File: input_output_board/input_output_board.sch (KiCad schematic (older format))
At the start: 18 parts, among them J1 Neutrik_NCJ6FA-H, J2 Neutrik_NCJ6FA-H, J3 Neutrik_NCJ6FA-H, J4 Neutrik_NCJ6FA-H, J5 Molex_SL_01x04_Male, J6 Conn_02x08_Odd_Even, J7 Molex_SL_01x04_Male, J8 AudioJack3, K1 G6S-2, K2 G6S-2, K3 G6S-2, K4 G6S-2, K5 G6S-2

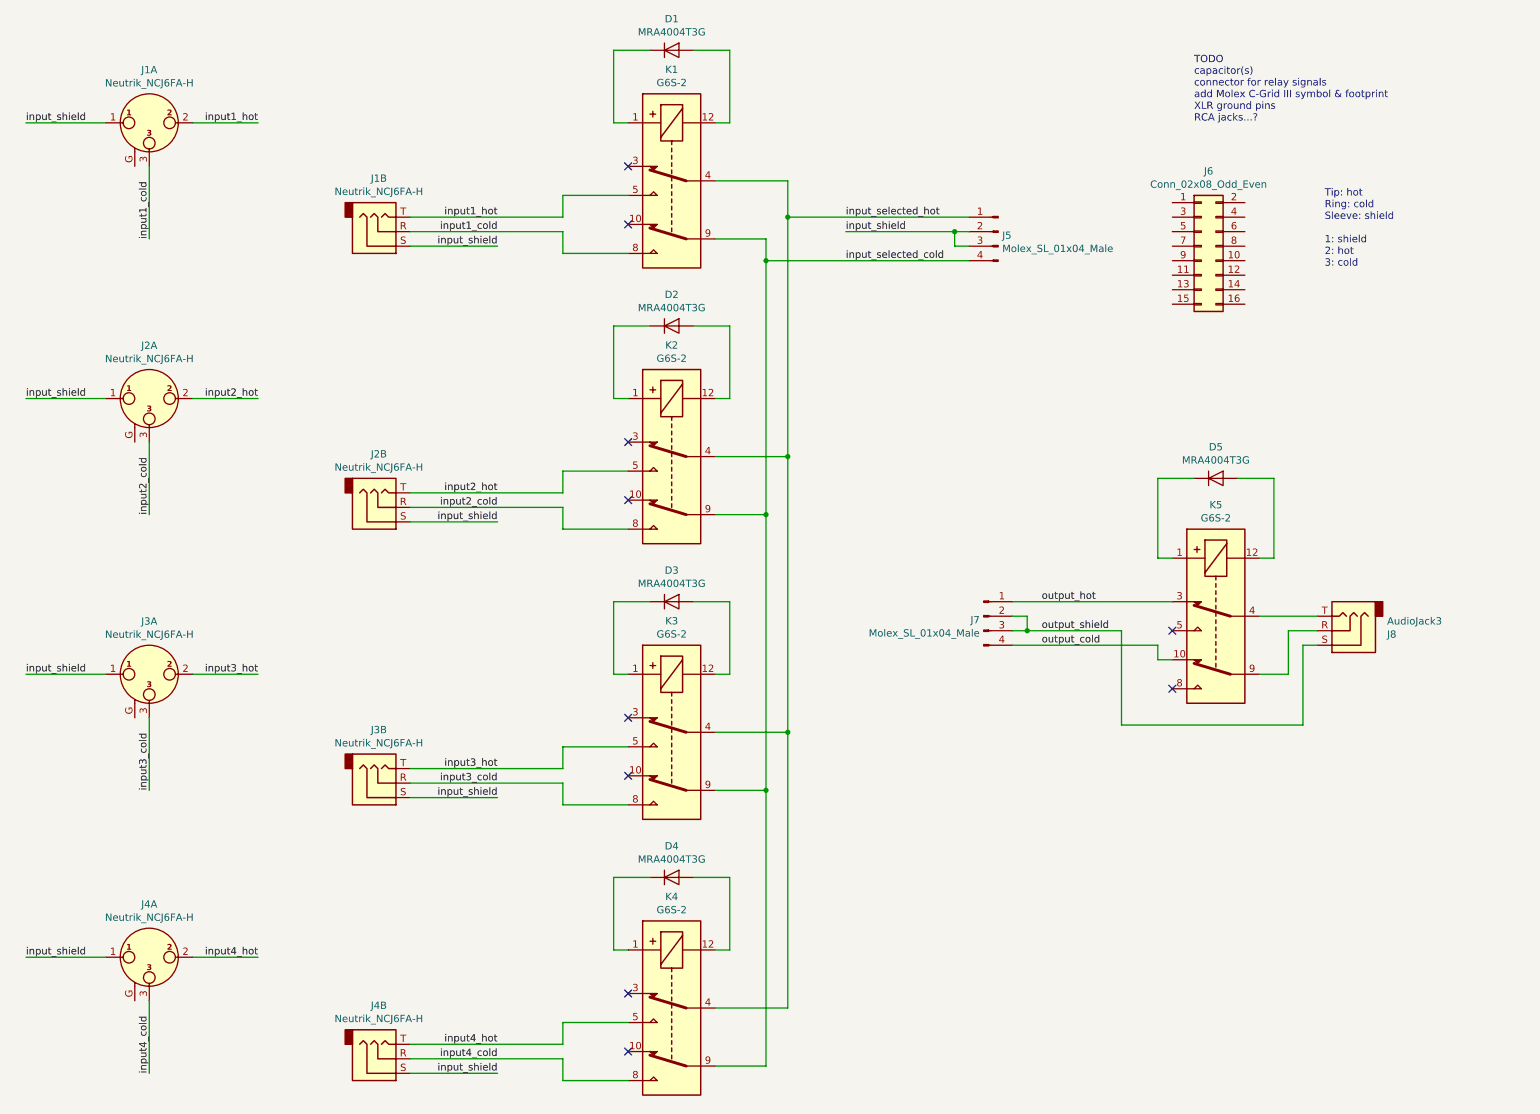
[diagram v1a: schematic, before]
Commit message: add relay power/ground connections
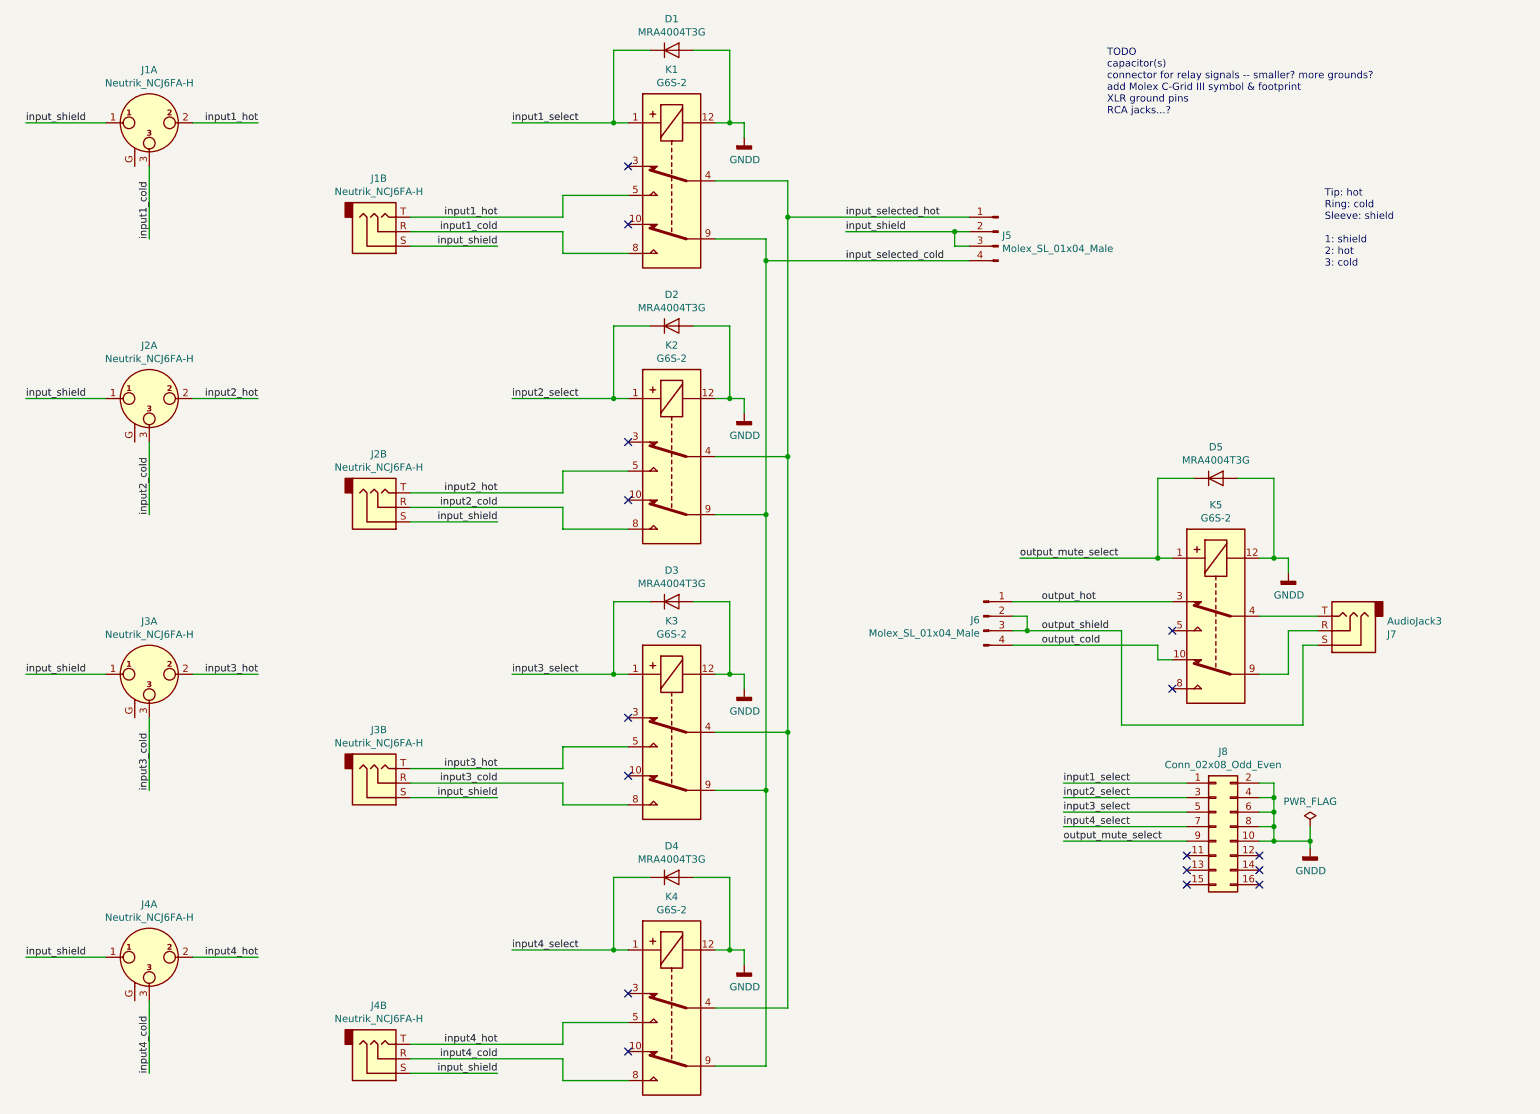
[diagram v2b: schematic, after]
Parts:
- renumbered J7 to J6, J8 to J7, J6 to J8
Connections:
- net input1_select: now reaches D1.1 (K), K1.1
- net input1_select: now also J8.1 (Pin_1)
- net GNDD: now reaches D1.2 (A), K1.12
- net GNDD: now also D2.2 (A), D3.2 (A), D4.2 (A), D5.2 (A), J8.10 (Pin_10), J8.2 (Pin_2), J8.4 (Pin_4), J8.6 (Pin_6), J8.8 (Pin_8), K2.12, K3.12, K4.12, K5.12
- net input2_select: now reaches D2.1 (K), K2.1
- net input2_select: now also J8.3 (Pin_3)
- net input3_select: now reaches D3.1 (K), K3.1
- net input3_select: now also J8.5 (Pin_5)
- net input4_select: now reaches D4.1 (K), K4.1
- net input4_select: now also J8.7 (Pin_7)
- net output_mute_select: now reaches J8.9 (Pin_9)
- net output_mute_select: now also D5.1 (K), K5.1
- no-connect marks 10 -> 16
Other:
- note added: "TODO\ncapacitor(s)\nconnector for relay signals -- smaller? more grounds?\nadd Molex C-Grid III symbol & footprint\nXLR ground pins\nRCA jacks...?"
- note removed: "TODO\ncapacitor(s)\nconnector for relay signals\nadd Molex C-Grid III symbol & footprint\nXLR ground pins\nRCA jacks...?"
- moved on the sheet: J8
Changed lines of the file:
@@
 $EndDescr
 $Comp
-L Connector:AudioJack3 J8
+L Connector:AudioJack3 J7
 U 1 1 5CAA8F23
 P 9750 4750
-F 0 "J8" H 9470 4775 50  0000 R CNN
+F 0 "J7" H 9470 4775 50  0000 R CNN
 F 1 "AudioJack3" H 9470 4684 50  0000 R CNN
 F 2 "" H 9750 4750 50  0001 C CNN
@@
 	5750 7750 5400 7750
 $Comp
-L Connector_gkeeth:Molex_SL_01x04_Male J7
+L Connector_gkeeth:Molex_SL_01x04_Male J6
 U 1 1 5CB5BBEB
 P 7250 4650
-F 0 "J7" H 7223 4624 50  0000 R CNN
+F 0 "J6" H 7223 4624 50  0000 R CNN
 F 1 "Molex_SL_01x04_Male" H 7223 4533 50  0000 R CNN
 F 2 "Connector_Molex_SL:Molex_SL_A-70543-0003_1x04_P2.54mm_Vertical" H 7250 4650 50  0001 C CNN
@@
 Text Label 7650 4750 0    50   ~ 0
 output_shield
-Text Notes 8700 1250 0    50   ~ 0
-TODO\ncapacitor(s)\nconnector for relay signals\nadd Molex C-Grid III symbol & footprint\nXLR ground pins\nRCA jacks...?
-$Comp
-L Connector_Generic:Conn_02x08_Odd_Even J6
+Text Notes 8100 1200 0    50   ~ 0
+TODO\ncapacitor(s)\nconnector for relay signals -- smaller? more grounds?\nadd Molex C-Grid III symbol & footprint\nXLR ground pins\nRCA jacks...?
+$Comp
+L Connector_Generic:Conn_02x08_Odd_Even J8
 U 1 1 5CB676D4
-P 8750 2100
-F 0 "J6" H 8800 2617 50  0000 C CNN
-F 1 "Conn_02x08_Odd_Even" H 8800 2526 50  0000 C CNN
-F 2 "" H 8750 2100 50  0001 C CNN
-F 3 "~" H 8750 2100 50  0001 C CNN
-	1    8750 2100
+P 8850 6100
+F 0 "J8" H 8900 6617 50  0000 C CNN
+F 1 "Conn_02x08_Odd_Even" H 8900 6526 50  0000 C CNN
+F 2 "" H 8850 6100 50  0001 C CNN
+F 3 "~" H 8850 6100 50  0001 C CNN
+	1    8850 6100
 	1    0    0    -1
 $EndComp
@@
 NoConn ~ 8550 5150
 NoConn ~ 8550 4750
+Wire Wire Line
+	8650 5800 7800 5800
+Wire Wire Line
+	8650 5900 7800 5900
+Wire Wire Line
+	8650 6000 7800 6000
+Wire Wire Line
+	8650 6100 7800 6100
+Text Label 7800 5800 0    50   ~ 0
+input1_select
+Text Label 7800 5900 0    50   ~ 0
+input2_select
+Text Label 7800 6000 0    50   ~ 0
+input3_select
+Text Label 7800 6100 0    50   ~ 0
+input4_select
+Wire Wire Line
+	9150 5800 9250 5800
+Wire Wire Line
+	9250 5800 9250 5900
+Wire Wire Line
+	9250 6100 9150 6100
+Wire Wire Line
+	9150 6000 9250 6000
+Connection ~ 9250 6000
+Wire Wire Line
+	9250 6000 9250 6100
+Wire Wire Line
+	9150 5900 9250 5900
+Connection ~ 9250 5900
+Wire Wire Line
+	9250 5900 9250 6000
+$Comp
+L power:GNDD #PWR0101
+U 1 1 5CCCC269
+P 9500 6250
+F 0 "#PWR0101" H 9500 6000 50  0001 C CNN
+F 1 "GNDD" H 9504 6095 50  0000 C CNN
+F 2 "" H 9500 6250 50  0001 C CNN
+F 3 "" H 9500 6250 50  0001 C CNN
+	1    9500 6250
+	1    0    0    -1
+$EndComp
+Wire Wire Line
+	9500 6250 9500 6200
+Wire Wire Line
+	9500 6200 9250 6200
+$Comp
+L power:GNDD #PWR0102
+U 1 1 5CCD0BDE
+P 5600 7050
+F 0 "#PWR0102" H 5600 6800 50  0001 C CNN
+F 1 "GNDD" H 5604 6895 50  0000 C CNN
+F 2 "" H 5600 7050 50  0001 C CNN
+F 3 "" H 5600 7050 50  0001 C CNN
+	1    5600 7050
+	1    0    0    -1
+$EndComp
+$Comp
+L power:GNDD #PWR0103
+U 1 1 5CCD13C1
+P 5600 5150
+F 0 "#PWR0103" H 5600 4900 50  0001 C CNN
+F 1 "GNDD" H 5604 4995 50  0000 C CNN
+F 2 "" H 5600 5150 50  0001 C CNN
+F 3 "" H 5600 5150 50  0001 C CNN
+	1    5600 5150
+	1    0    0    -1
+$EndComp
+$Comp
+L power:GNDD #PWR0104
+U 1 1 5CCD19F8
+P 5600 3250
+F 0 "#PWR0104" H 5600 3000 50  0001 C CNN
+F 1 "GNDD" H 5604 3095 50  0000 C CNN
+F 2 "" H 5600 3250 50  0001 C CNN
+F 3 "" H 5600 3250 50  0001 C CNN
+	1    5600 3250
+	1    0    0    -1
+$EndComp
+$Comp
+L power:GNDD #PWR0105
+U 1 1 5CCD1DD8
+P 5600 1350
+F 0 "#PWR0105" H 5600 1100 50  0001 C CNN
+F 1 "GNDD" H 5604 1195 50  0000 C CNN
+F 2 "" H 5600 1350 50  0001 C CNN
+F 3 "" H 5600 1350 50  0001 C CNN
+	1    5600 1350
+	1    0    0    -1
+$EndComp
+$Comp
+L power:GNDD #PWR0106
+U 1 1 5CCD2277
+P 9350 4350
+F 0 "#PWR0106" H 9350 4100 50  0001 C CNN
+F 1 "GNDD" H 9354 4195 50  0000 C CNN
+F 2 "" H 9350 4350 50  0001 C CNN
+F 3 "" H 9350 4350 50  0001 C CNN
+	1    9350 4350
+	1    0    0    -1
+$EndComp
+Wire Wire Line
+	9350 4350 9350 4250
+Wire Wire Line
+	9350 4250 9250 4250
+Connection ~ 9250 4250
+Wire Wire Line
+	5600 5150 5600 5050
+Wire Wire Line
+	5600 5050 5500 5050
+Connection ~ 5500 5050
+Wire Wire Line
+	5600 7050 5600 6950
+Wire Wire Line
+	5600 6950 5500 6950
+Connection ~ 5500 6950
+Wire Wire Line
+	5600 3250 5600 3150
+Wire Wire Line
+	5600 3150 5500 3150
+Connection ~ 5500 3150
+Wire Wire Line
+	5600 1350 5600 1250
+Wire Wire Line
+	5600 1250 5500 1250
+Connection ~ 5500 1250
+Text Label 4000 1250 0    50   ~ 0
+input1_select
+Text Label 4000 3150 0    50   ~ 0
+input2_select
+Text Label 4000 5050 0    50   ~ 0
+input3_select
+Text Label 4000 6950 0    50   ~ 0
+input4_select
+Text Label 7800 6200 0    50   ~ 0
+output_mute_select
+Wire Wire Line
+	7800 6200 8650 6200
+Wire Wire Line
+	9250 6200 9250 6100
+Connection ~ 9250 6100
+Wire Wire Line
+	9250 6200 9150 6200
+Connection ~ 9250 6200
+Text Label 7500 4250 0    50   ~ 0
+output_mute_select
+Wire Wire Line
+	7500 4250 8450 4250
+Connection ~ 8450 4250
+Wire Wire Line
+	4700 5050 4000 5050
+Connection ~ 4700 5050
+Wire Wire Line
+	4000 3150 4700 3150
+Connection ~ 4700 3150
+Wire Wire Line
+	4000 1250 4700 1250
+Connection ~ 4700 1250
+Wire Wire Line
+	4000 6950 4700 6950
+Connection ~ 4700 6950
+NoConn ~ 8650 6300
+NoConn ~ 8650 6400
+NoConn ~ 8650 6500
+NoConn ~ 9150 6300
+NoConn ~ 9150 6400
+NoConn ~ 9150 6500
+$Comp
+L power:PWR_FLAG #FLG0101
+U 1 1 5CD4A6A5
+P 9500 6100
+F 0 "#FLG0101" H 9500 6175 50  0001 C CNN
+F 1 "PWR_FLAG" H 9500 6273 50  0000 C CNN
+F 2 "" H 9500 6100 50  0001 C CNN
+F 3 "~" H 9500 6100 50  0001 C CNN
+	1    9500 6100
+	1    0    0    -1
+$EndComp
+Wire Wire Line
+	9500 6200 9500 6100
+Connection ~ 9500 6200
 $EndSCHEMATC

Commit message: redraw input jack/relay circuits
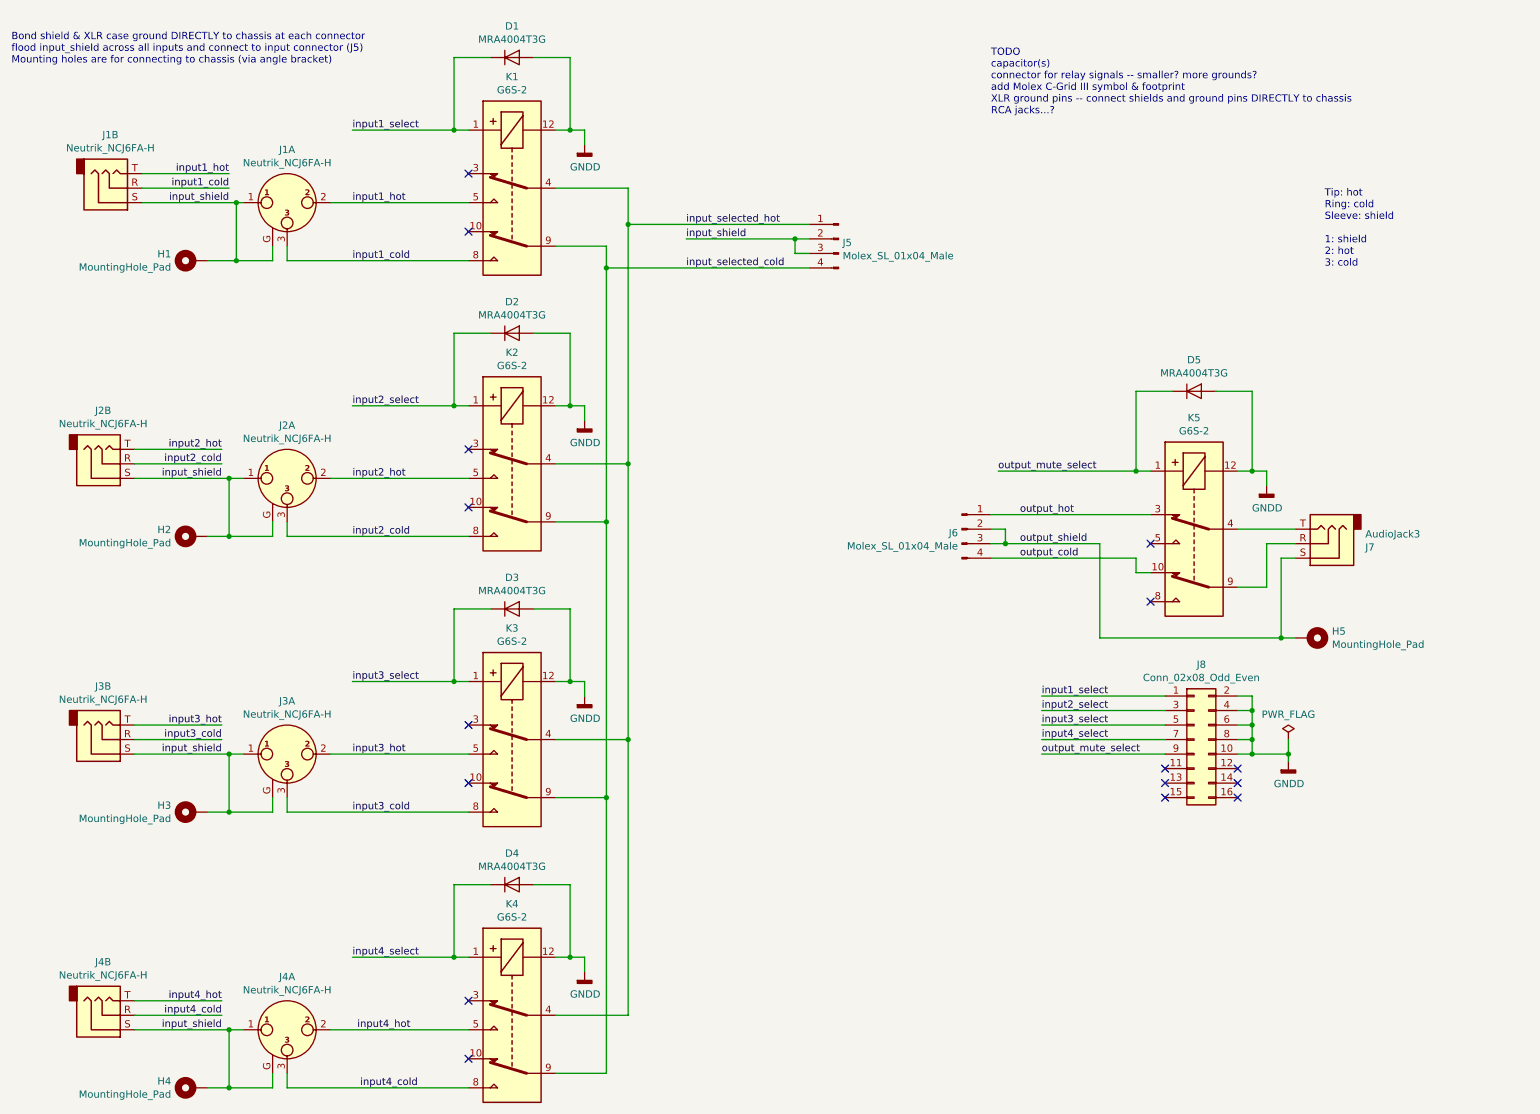
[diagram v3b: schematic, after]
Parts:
- added H1, H2, H3, H4, H5: MountingHole_Pad, symbol Mechanical:MountingHole_Pad
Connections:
- net input_shield: now also J1.G, J2.G, J3.G, J4.G, H1.1, H2.1, H3.1, H4.1
- net output_shield: now also H5.1
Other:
- note added: "Bond shield & XLR case ground DIRECTLY to chassis at each connector\nflood input_shield across all inputs and connect to input connector (J5)\nMounting holes are for connecting to chassis (via angle bracket)"
- note added: "TODO\ncapacitor(s)\nconnector for relay signals -- smaller? more grounds?\nadd Molex C-Grid III symbol & footprint\nXLR ground pins -- connect shields and ground pins DIRECTLY to chassis\nRCA jacks...?"
- note removed: "TODO\ncapacitor(s)\nconnector for relay signals -- smaller? more grounds?\nadd Molex C-Grid III symbol & footprint\nXLR ground pins\nRCA jacks...?"
- moved on the sheet: D1, D2, D3, D4, D5, J1A, J1B, J2A, J2B, J3A, J3B, J4A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

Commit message: reorganize schematic and add graphic organization
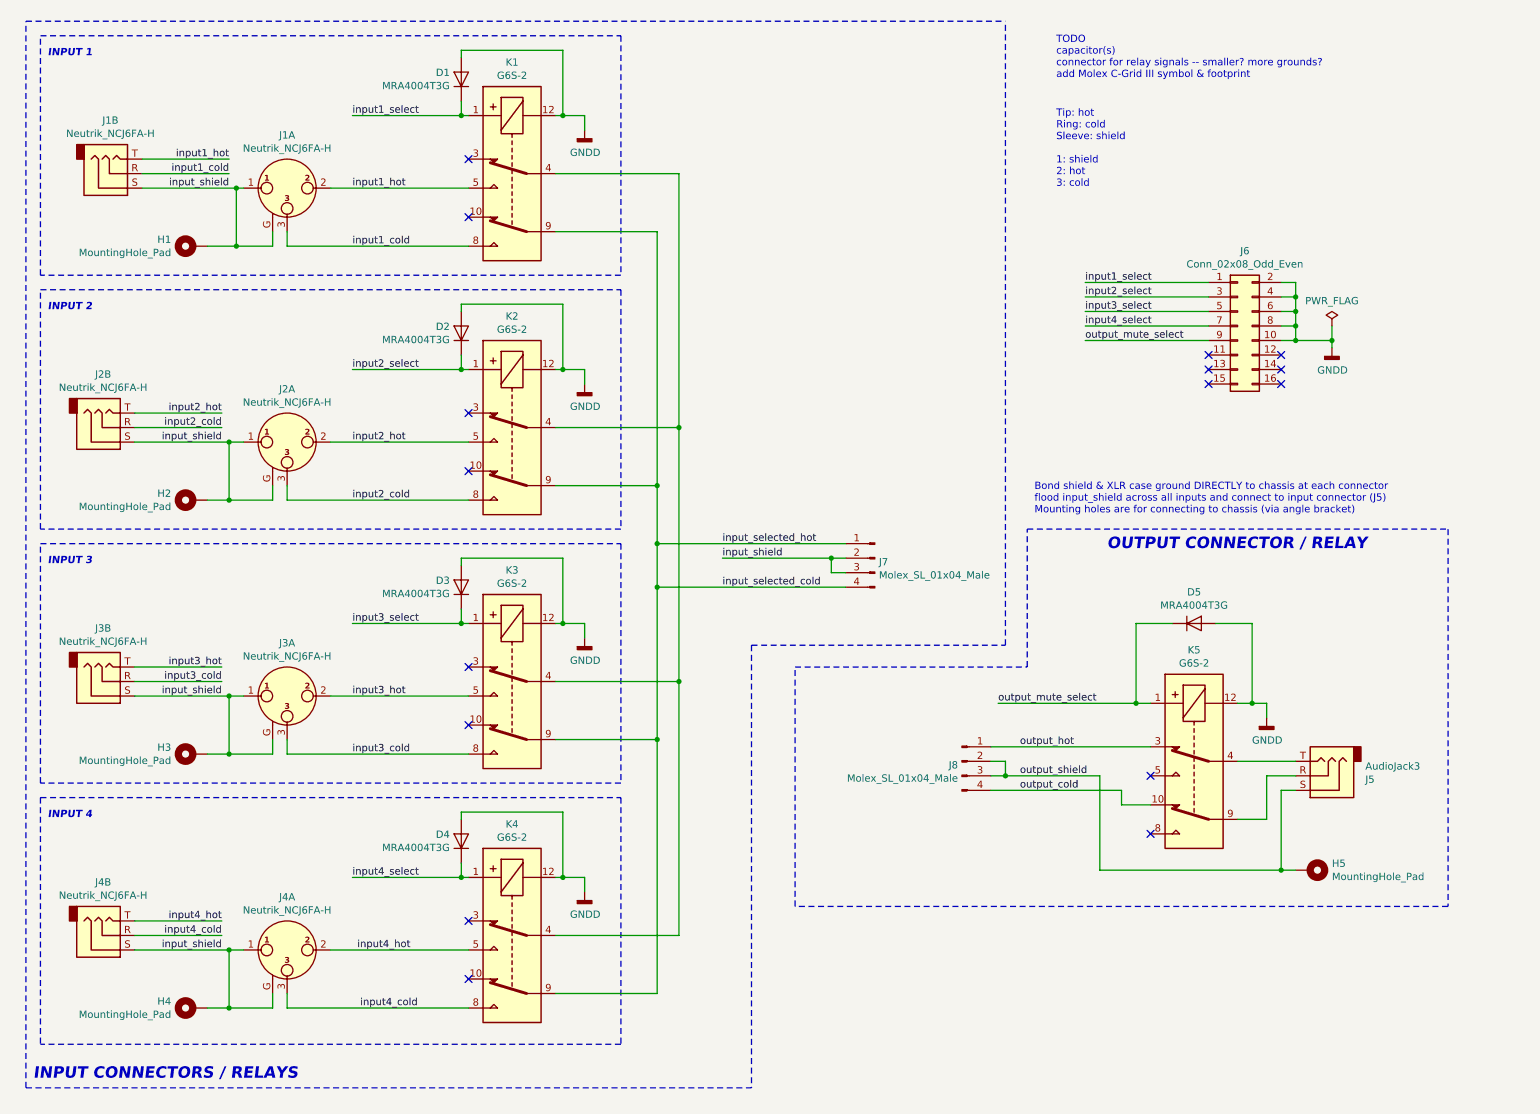
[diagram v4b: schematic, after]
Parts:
- renumbered J7 to J5, J8 to J6, J5 to J7, J6 to J8
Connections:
- net input_selected_cold: now also J7.1 (Pin_1)
- net input_selected_hot: no longer names the net of K1.4, K2.4, K3.4, K4.4
- net input_selected_hot: no longer J7.1 (Pin_1)
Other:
- note added: "INPUT 1"
- note added: "INPUT 2"
- note added: "INPUT 3"
- note added: "INPUT 4"
- note added: "INPUT CONNECTORS / RELAYS"
- note added: "OUTPUT CONNECTOR / RELAY"
- note added: "TODO\ncapacitor(s)\nconnector for relay signals -- smaller? more grounds?\nadd Molex C-Grid III symbol & footprint"
- note removed: "TODO\ncapacitor(s)\nconnector for relay signals -- smaller? more grounds?\nadd Molex C-Grid III symbol & footprint\nXLR ground pins -- connect shields and ground pins DIRECTLY to chassis\nRCA jacks...?"
- moved on the sheet: D1, D2, D3, D4, D5, H1, H2, H3, H4, H5, J1A, J1B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
